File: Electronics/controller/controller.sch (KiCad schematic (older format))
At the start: 25 parts, among them P1 POWER, P2 PANEL_1, P3 PANEL_2, Q1 FET, SW1 SW_PUSH, U1 LM317T, U2 74HC595, U3 Arduino_Pro_Micro

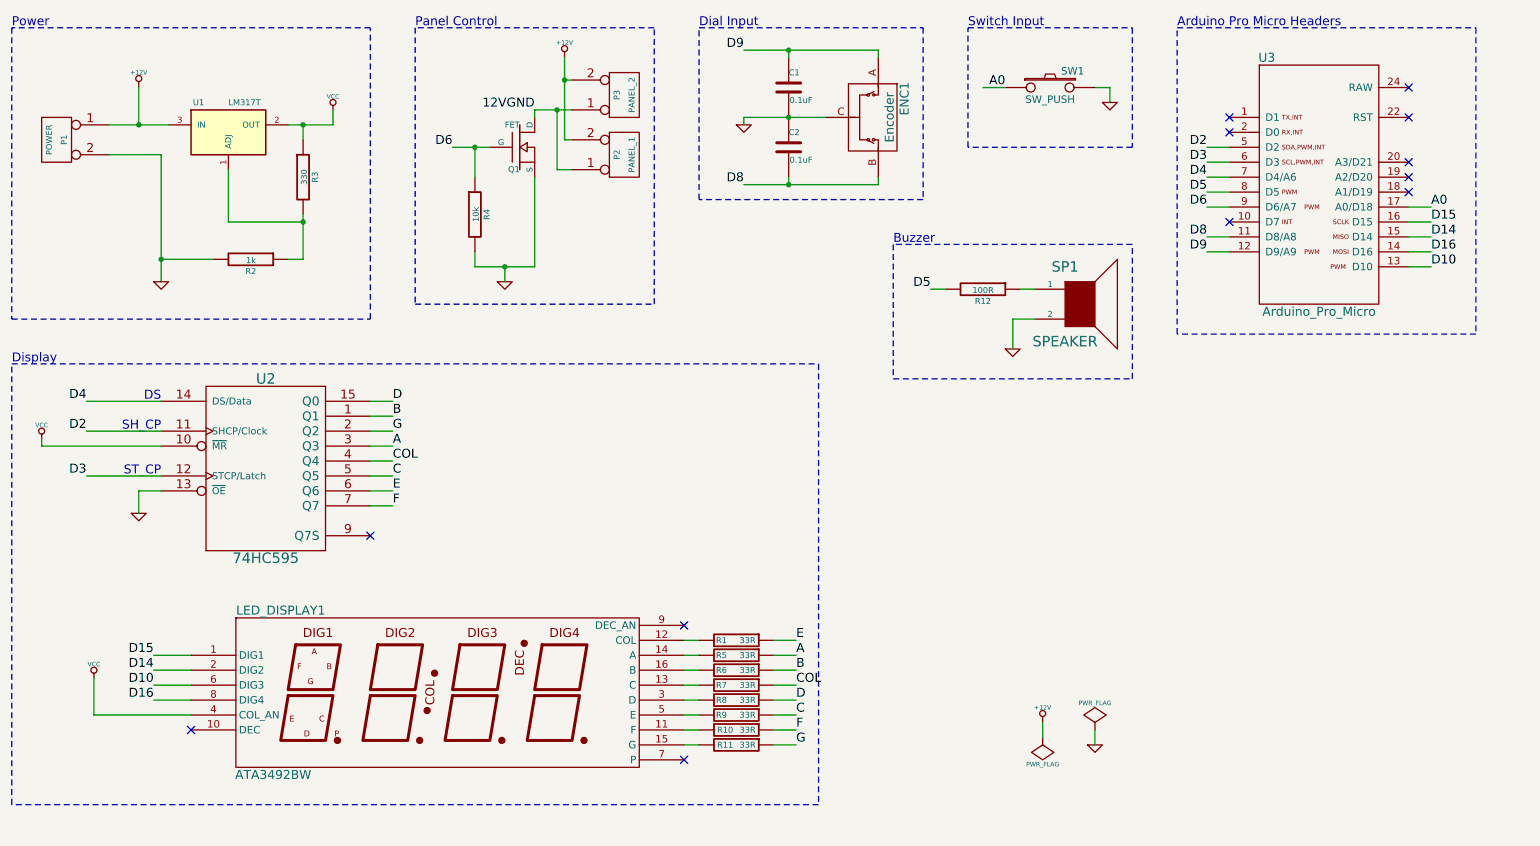
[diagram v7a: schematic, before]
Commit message: Updated schematics after prototype testing.
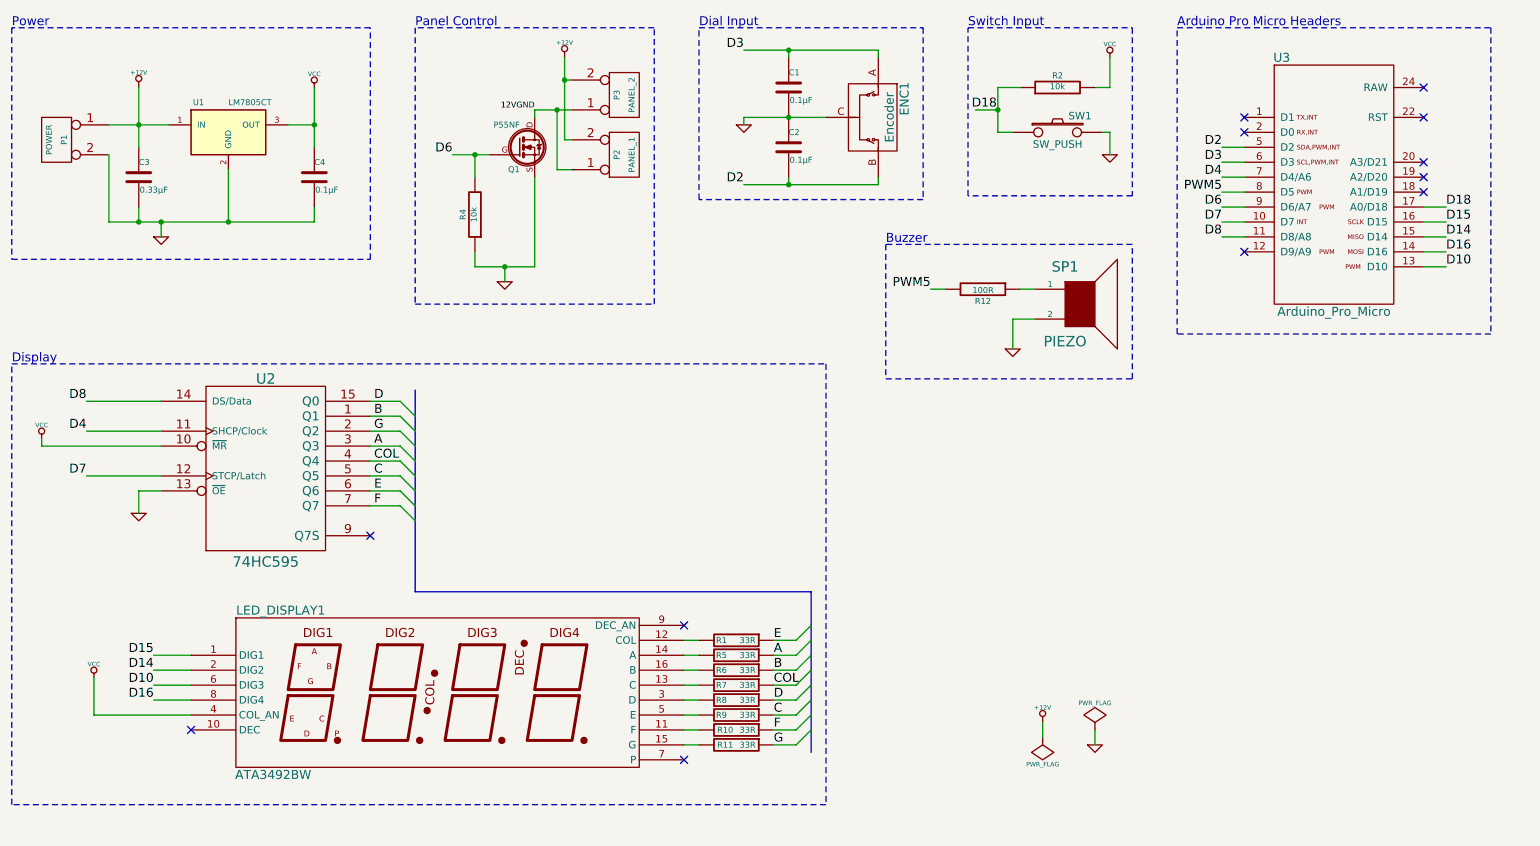
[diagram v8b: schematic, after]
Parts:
- removed Q1: FET, Transistors_TO-220:TO-220_FET-GDS_Vertical, symbol MOSFET_N
- removed R3: 330, Discret:R3, symbol R
- removed U1: LM317T, Transistors_TO-220:TO-220_Neutral123_Horizontal, symbol LM317T
- added C3: 0.33µF, Capacitors_ThroughHole:Capacitor4x3RM2.5, symbol C
- added C4: 0.1µF, Capacitors_ThroughHole:Capacitor4x3RM2.5, symbol C
- added Q1: P55NF, Transistors_TO-220:TO-220_FET-GDS_Horizontal, symbol STB55NF
- added U1: LM7805CT, Transistors_TO-220:TO-220_Neutral123_Horizontal, symbol LM7805CT
- C1, C2: value 0.1uF -> 0.1µF
- R2: value 1k -> 10k
- SP1: value SPEAKER -> PIEZO
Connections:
- net +12V: now also C3.1, U1.1 (IN)
- net 12VGND: now also Q1.D
- net D2: now also C2.2, ENC1.B; no longer U2.11 (SHCP/Clock)
- net D3: now also C1.1, ENC1.A; no longer U2.12 (STCP/Latch)
- net D4: now also U2.11 (SHCP/Clock); no longer U2.14 (DS/Data)
- net D6: now also R4.2, Q1.G; no longer R4.1
- net D8: now also U2.14 (DS/Data); no longer C2.2, ENC1.B
- net GND: now also R4.1, C3.2, C4.2, Q1.S, U1.2 (GND); no longer R2.2, R4.2
- net VCC: now also R2.2, C4.1, U1.3 (OUT)
- net at R2.1: now also SW1.1
- net D7: now reaches U3.10 (D7)
- net D7: now also U2.12 (STCP/Latch)
- net A0 renamed D18
- net D18: no longer SW1.1
- net D5 renamed PWM5
- removed net D9: C1.1, ENC1.A, U3.12 (D9/A9)
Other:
- note removed: "DS"
- note removed: "SH_CP"
- note removed: "ST_CP"
- moved on the sheet: SW1, U3
